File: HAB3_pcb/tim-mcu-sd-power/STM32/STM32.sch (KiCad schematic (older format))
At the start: 40 parts, among them J1 Conn_ARM_JTAG_SWD_20, J2 Micro_SD_Card_Det, J3 Conn_01x16_Male, J4 Conn_01x16_Male, J5 Conn_01x16_Male, J6 Conn_01x02_Male, J7 Conn_01x02_Male, J8 Conn_01x02_Male, J9 Conn_01x11_Male, SW1 SW_DPST_x2, U1 STM32F401RET6, U2 LD3985M33R_SOT23, Y1 32.768MHz

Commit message: halfway done with  power regulator
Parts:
- added C? (x13): C, symbol C
- added J?: Conn_01x05_Male, symbol Conn_01x05_Male
- added L? (x2): L, symbol L
- added R? (x7): R, symbol R
- added U?: TPS65270PWPR, symbol TPS65270PWPR
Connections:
- net +3V3: now also C?.1, C?.1, J?.2 (Pin_2), L?.1, R?.2
- net GND: now also C?.1, C?.1, C?.1, C?.1, C?.1, C?.1, C?.1, C?.2, C?.2, J?.4 (Pin_4), J?.5 (Pin_5), R?.1, R?.2, R?.2, U?.17 (GND), U?.18 (GND), U?.19 (GND), U?.20 (GND), U?.5 (LOW_P), U?.7 (AGND)
- new net: C?.2, U?.10 (SS2)
- new net: C?.1, U?.13 (BST2)
- new net: C?.2, L?.2, U?.15 (LX2), U?.16 (LX2)
- new net: C?.2, L?.2, U?.21 (LX1), U?.22 (LX1)
- new net: C?.1, U?.24 (BS1)
- new net: C?.2, U?.3 (SS1)
- new net: R?.1, U?.4 (COMP1)
- new net: C?.2, U?.6 (VCC)
- new net: R?.1, U?.8 (ROSC)
- new net: R?.1, U?.9 (COMP2)
- new net: C?.2, R?.2 (x2)
- new net: R?.1, R?.2 (x2)
- new net +5V: C?.2, C?.2, J?.3 (Pin_3), L?.1, R?.1
- new net +7.5V: C?.1, C?.2, J?.1 (Pin_1), U?.1 (EN1), U?.12 (EN2), U?.14 (VIN2), U?.23 (VIN1)
- new net FB1: C?.1, U?.2 (FB1)
- new net FB2: C?.2, U?.11 (FB2)

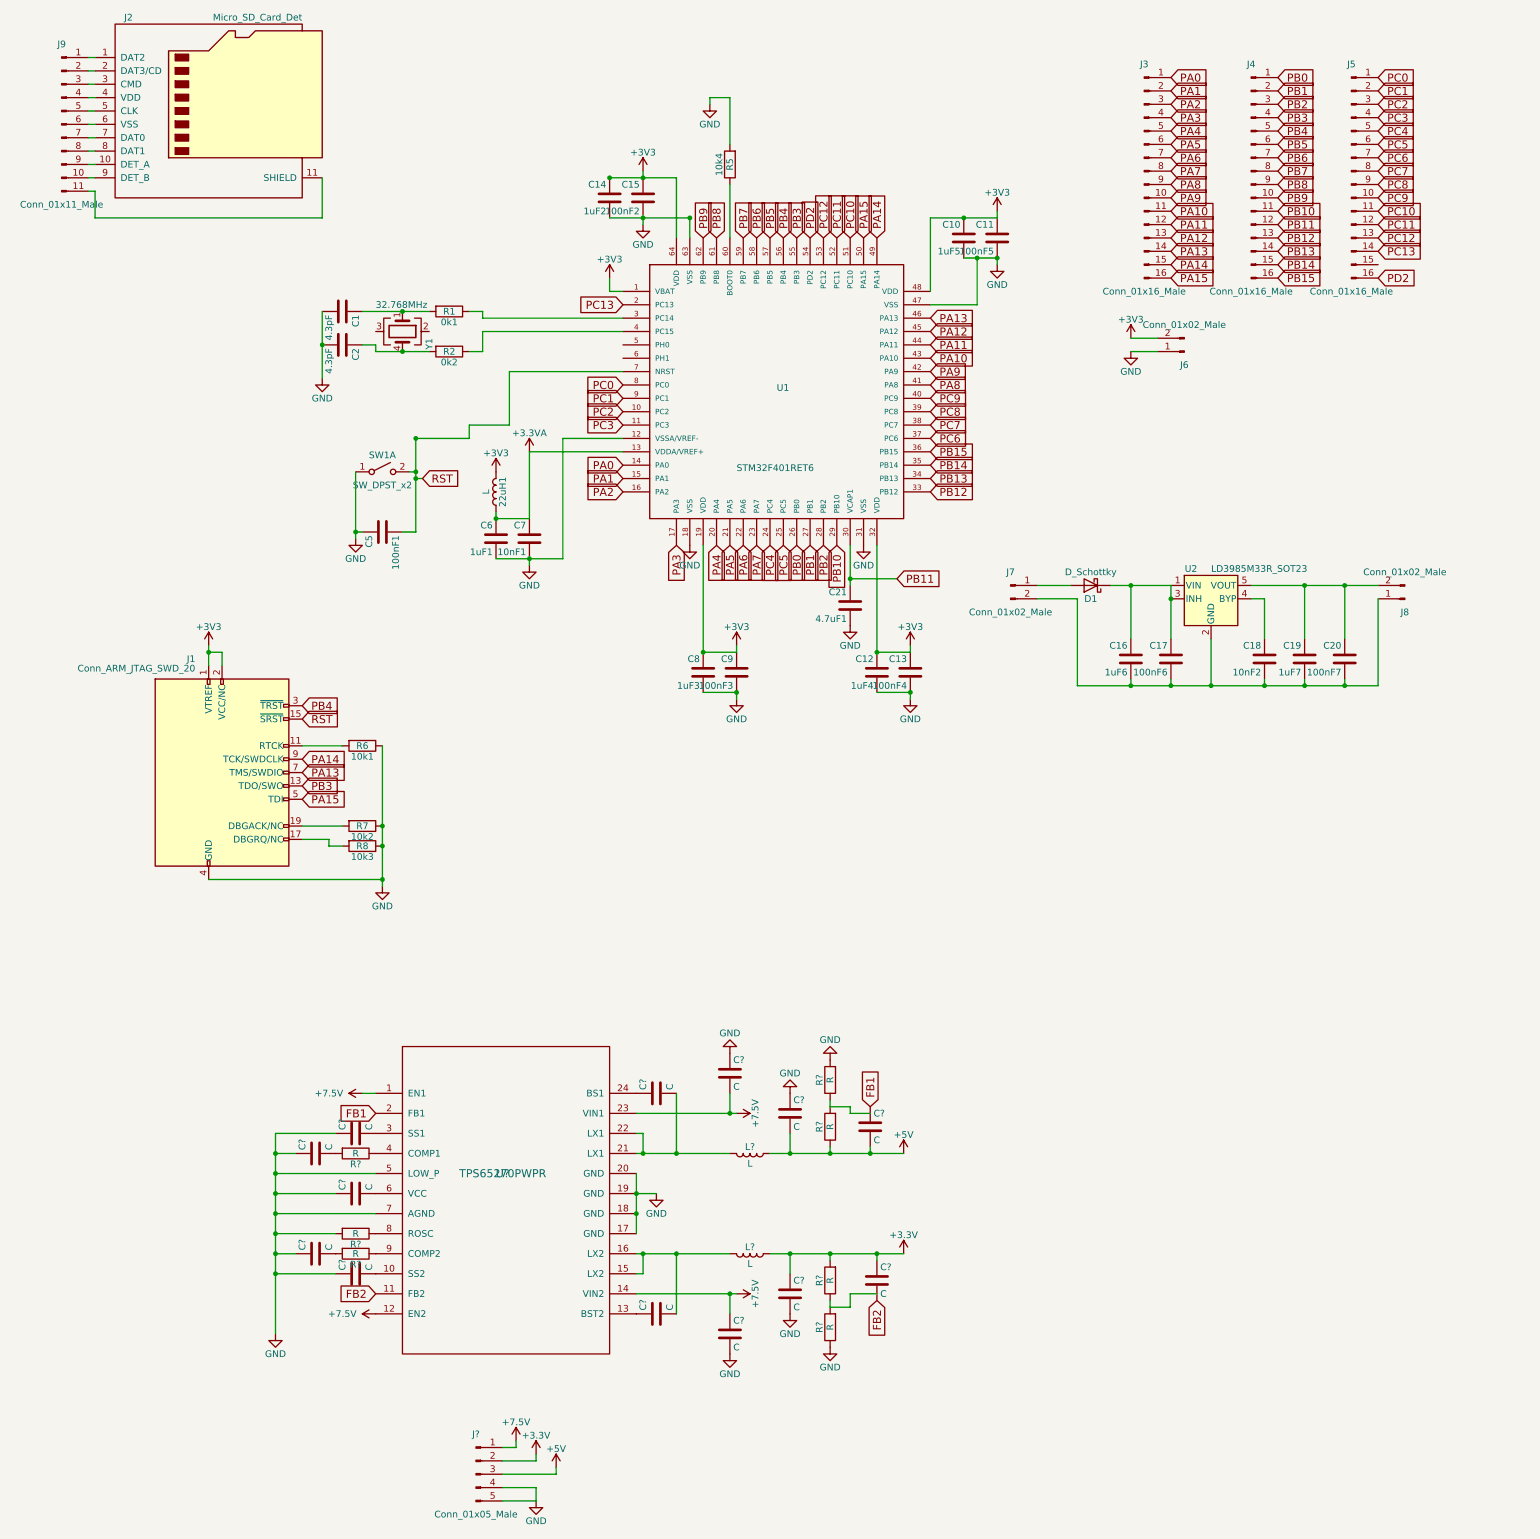
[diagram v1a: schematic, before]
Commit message: Finished voltage regulator
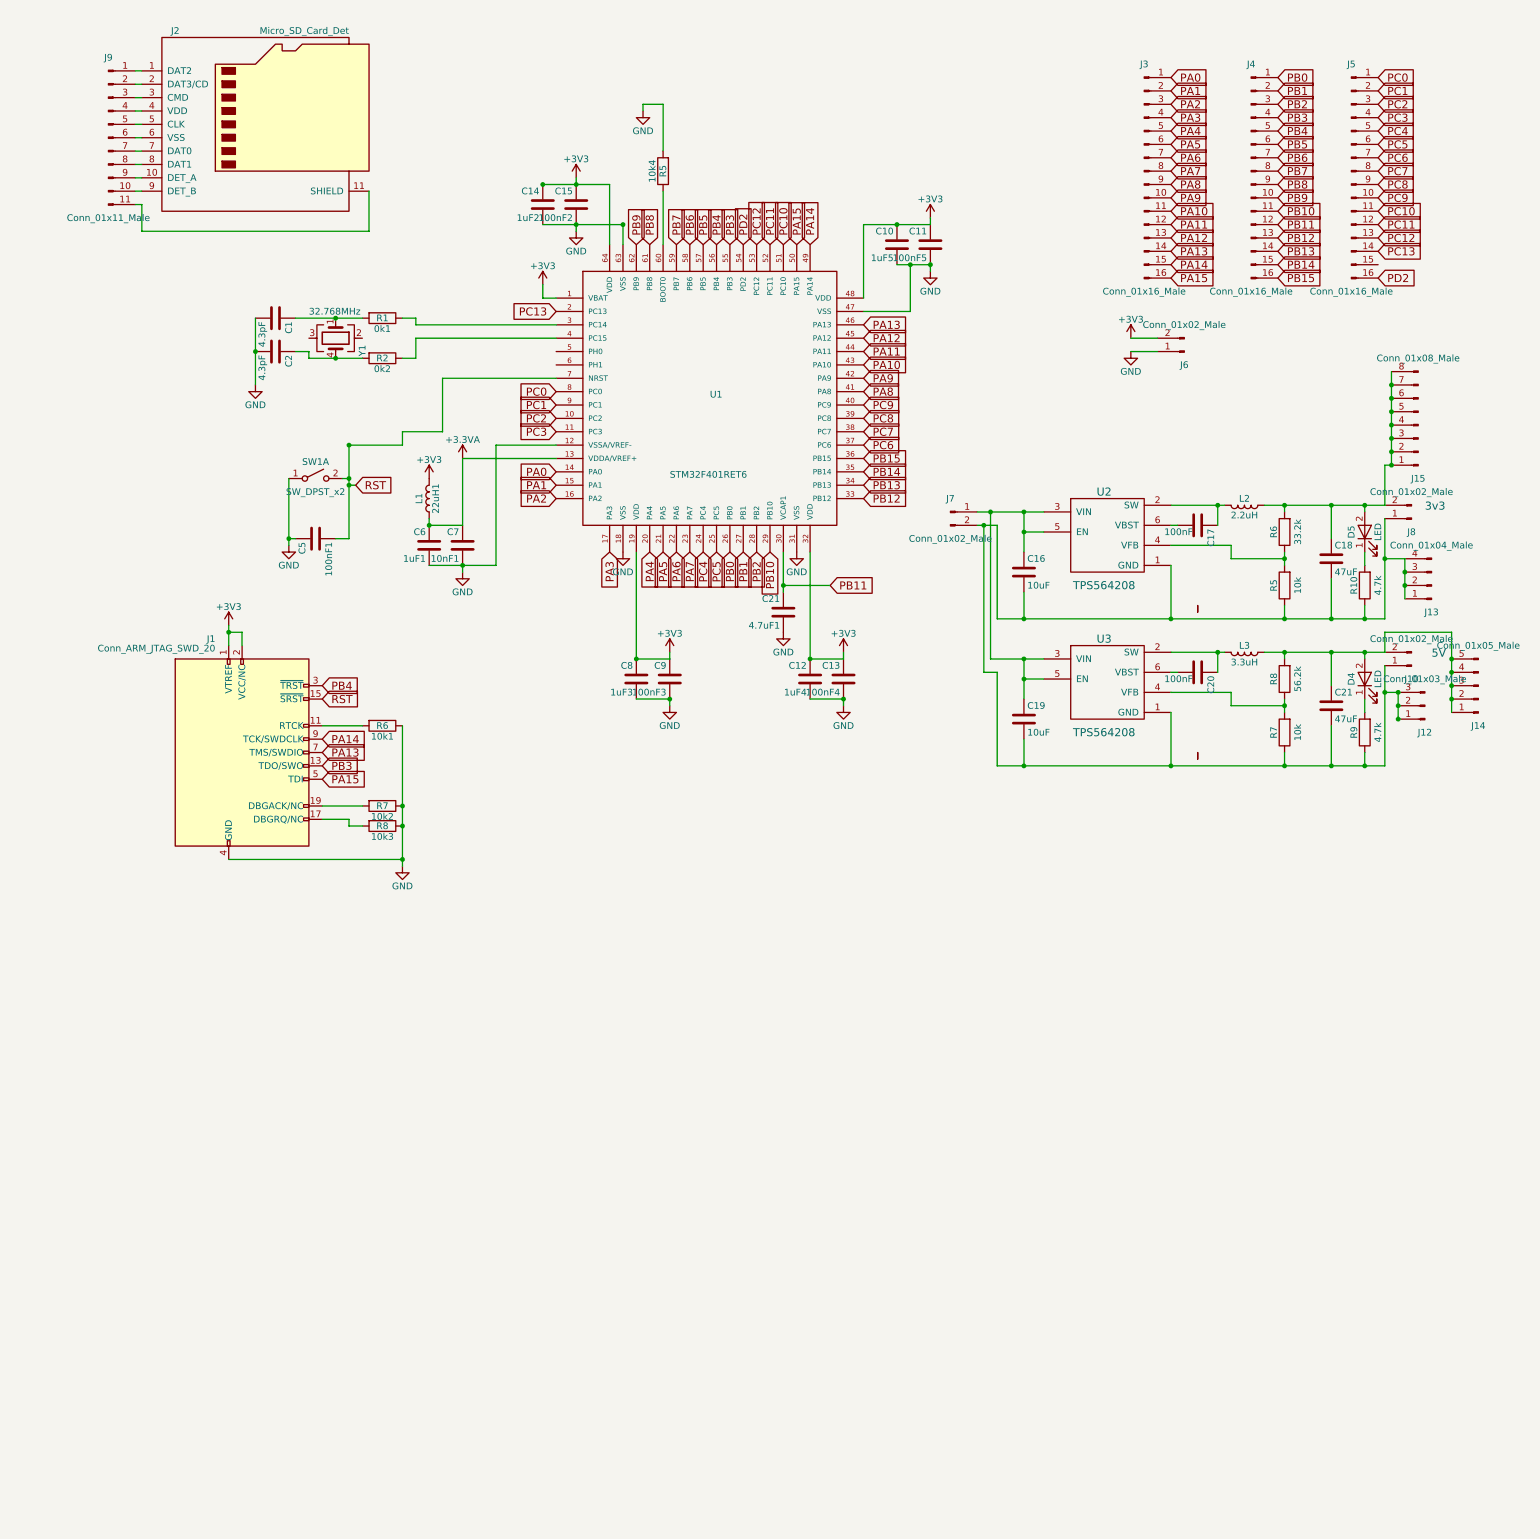
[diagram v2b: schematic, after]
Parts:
- removed 100nF6: C17, Capacitors_SMD:C_0603_HandSoldering, symbol C
- removed 100nF7: C20, Capacitors_SMD:C_0603_HandSoldering, symbol C
- removed 10nF2: C18, Capacitors_SMD:C_0603_HandSoldering, symbol C
- removed 1uF6: C16, Capacitors_SMD:C_0603_HandSoldering, symbol C
- removed 1uF7: C19, Capacitors_SMD:C_0603_HandSoldering, symbol C
- removed C? (x13): C, symbol C
- removed D1: D_Schottky, Diodes_SMD:D_SOD-323_HandSoldering, symbol D_Schottky
- removed J?: Conn_01x05_Male, symbol Conn_01x05_Male
- removed L? (x2): L, symbol L
- removed R? (x7): R, symbol R
- removed U2: LD3985M33R_SOT23, TO_SOT_Packages_SMD:SOT-23-5, symbol LD3985M33R_SOT23
- removed U?: TPS65270PWPR, symbol TPS65270PWPR
- added C16, C19: 10uF, Capacitors_SMD:C_0603_HandSoldering, symbol C
- added C17, C20: 100nF, Capacitors_SMD:C_0603_HandSoldering, symbol C
- added C18, C21: 47uF, Capacitors_SMD:C_0603_HandSoldering, symbol C
- added D4, D5: LED, LEDs:LED_0603_HandSoldering, symbol LED
- added J10: Conn_01x02_Male, Pin_Headers:Pin_Header_Straight_1x02_Pitch2.54mm, symbol Conn_01x02_Male
- added J12: Conn_01x03_Male, Pin_Headers:Pin_Header_Straight_1x03_Pitch2.54mm, symbol Conn_01x03_Male
- added J13: Conn_01x04_Male, Pin_Headers:Pin_Header_Straight_1x04_Pitch2.54mm, symbol Conn_01x04_Male
- added J14: Conn_01x05_Male, Pin_Headers:Pin_Header_Straight_1x05_Pitch2.54mm, symbol Conn_01x05_Male
- added J15: Conn_01x08_Male, Pin_Headers:Pin_Header_Straight_1x08_Pitch2.54mm, symbol Conn_01x08_Male
- added L2: 2.2uH, TPS564208:INDC7070X450, symbol L
- added L3: 3.3uH, TPS564208:INDC7070X450, symbol L
- added R10, R9: 4.7k, Resistors_SMD:R_0603_HandSoldering, symbol R
- added R5, R7: 10k, Resistors_SMD:R_0603_HandSoldering, symbol R
- added R6: 33.2k, Resistors_SMD:R_0603_HandSoldering, symbol R
- added R8: 56.2k, Resistors_SMD:R_0603_HandSoldering, symbol R
- added U2, U3: TPS564208, TPS564208:TPS564208, symbol TPS564208
- 22uH1: value L -> L1
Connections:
- net at J7.1 (Pin_1): now also C16.1, C19.1, U2.3 (VIN), U2.5 (EN), U3.3 (VIN), U3.5 (EN)
- net at J7.2 (Pin_2), J8.1 (Pin_1): now also C16.2, C18.2, C19.2, C21.2, J10.1 (Pin_1), J12.1 (Pin_1), J12.2 (Pin_2), J12.3 (Pin_3), J13.1 (Pin_1), J13.2 (Pin_2), J13.3 (Pin_3), J13.4 (Pin_4), R10.1, R5.1, R7.1, R9.1, U2.1 (GND), U3.1 (GND)
- net at J8.2 (Pin_2): now also C18.1, D5.2 (A), J15.1 (Pin_1), J15.2 (Pin_2), J15.3 (Pin_3), J15.4 (Pin_4), J15.5 (Pin_5), J15.6 (Pin_6), J15.7 (Pin_7), J15.8 (Pin_8), L2.1, R6.2
- new net: C17.1, L2.2, U2.2 (SW)
- new net: R5.2, R6.1, U2.4 (VFB)
- new net: C17.2, U2.6 (VBST)
- new net: C20.1, L3.2, U3.2 (SW)
- new net: R7.2, R8.1, U3.4 (VFB)
- new net: C20.2, U3.6 (VBST)
- new net: C21.1, D4.2 (A), J10.2 (Pin_2), J14.1 (Pin_1), J14.2 (Pin_2), J14.3 (Pin_3), J14.4 (Pin_4), J14.5 (Pin_5), L3.1, R8.2
- new net: D4.1 (K), R9.2
- new net: D5.1 (K), R10.2
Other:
- note added: "3v3"
- note added: "5V"
- moved on the sheet: 0k1, 0k2, 100nF1, 100nF2, 100nF3, 100nF4, 100nF5, 10k1, 10k2, 10k3, 10k4, 10nF1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

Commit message: commit unsaved changes
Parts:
- 0k1, 0k2, 10k1, 10k2, 10k3, 10k4, R10, R5, R6, R7, R8, R9: symbol R -> STM32-rescue:R
- 100nF1, 100nF2, 100nF3, 100nF4, 100nF5, 10nF1, 1uF1, 1uF2, 1uF3, 1uF4, 1uF5, 4.7uF1, C1, C16, C17, C18, C19, C2, C20, C21: symbol C -> STM32-rescue:C
- 22uH1, L2, L3: symbol L -> STM32-rescue:L
- D4, D5: symbol LED -> STM32-rescue:LED
- J1: symbol Conn_ARM_JTAG_SWD_20 -> STM32-rescue:Conn_ARM_JTAG_SWD_20
- J10, J6, J7, J8: symbol Conn_01x02_Male -> STM32-rescue:Conn_01x02_Male
- J12: symbol Conn_01x03_Male -> STM32-rescue:Conn_01x03_Male
- J13: symbol Conn_01x04_Male -> STM32-rescue:Conn_01x04_Male
- J14: symbol Conn_01x05_Male -> STM32-rescue:Conn_01x05_Male
- J15: symbol Conn_01x08_Male -> STM32-rescue:Conn_01x08_Male
- J2: symbol Micro_SD_Card_Det -> STM32-rescue:Micro_SD_Card_Det
- J3, J4, J5: symbol Conn_01x16_Male -> STM32-rescue:Conn_01x16_Male
- J9: symbol Conn_01x11_Male -> STM32-rescue:Conn_01x11_Male
- SW1: symbol SW_DPST_x2 -> STM32-rescue:SW_DPST_x2
- U1: symbol STM32F401RET6 -> STM32-rescue:STM32F401RET6
- U2, U3: symbol TPS564208 -> STM32-rescue:TPS564208
- Y1: symbol Crystal_GND23 -> STM32-rescue:Crystal_GND23
